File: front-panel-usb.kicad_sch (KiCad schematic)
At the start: 107 parts, among them J4 USB-C_Kycon_KUSBX-SL2-CS1N24-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, J5 Tag-Connect_TC2050-IDC-NL_2x5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, J6 USB-C_Kycon_KUSBX-SL2-CS1N24-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, J7 USB-C_Kycon_KUSBX-SL2-CS1N24-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, Q1 PJE138K, U11 TPD4E05U06QDQARQ1, U12 FT4232H_VQFN, U13 NCP718BSN330T1G, U14 74LVC06ABQ, U15 AP22615B_TSOT26, U16 AP22615B_TSOT26, U17 FUSB303B, U18 FUSB303B, U19 TPD4E05U06QDQARQ1, U20 TPD4E05U06QDQARQ1, Y3 Resonator_12MHz_ABM8G

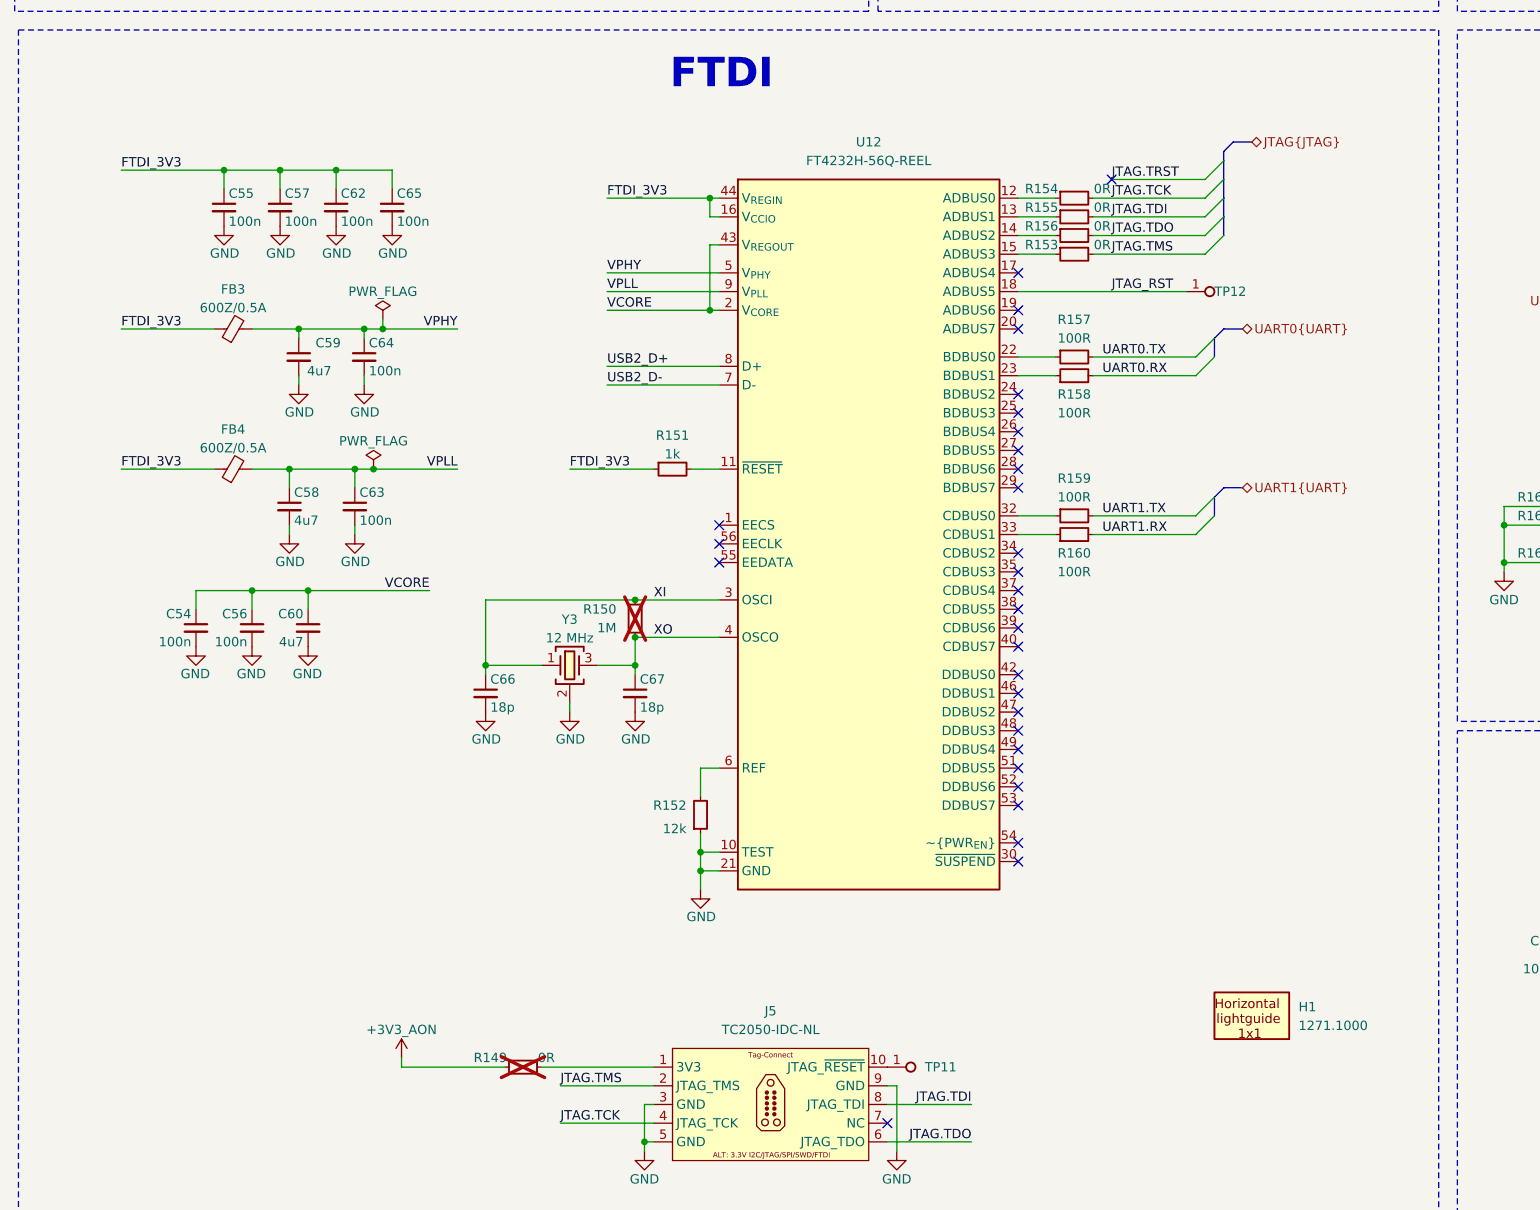
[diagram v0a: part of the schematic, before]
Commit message: [#83767] Add alternative reset signal
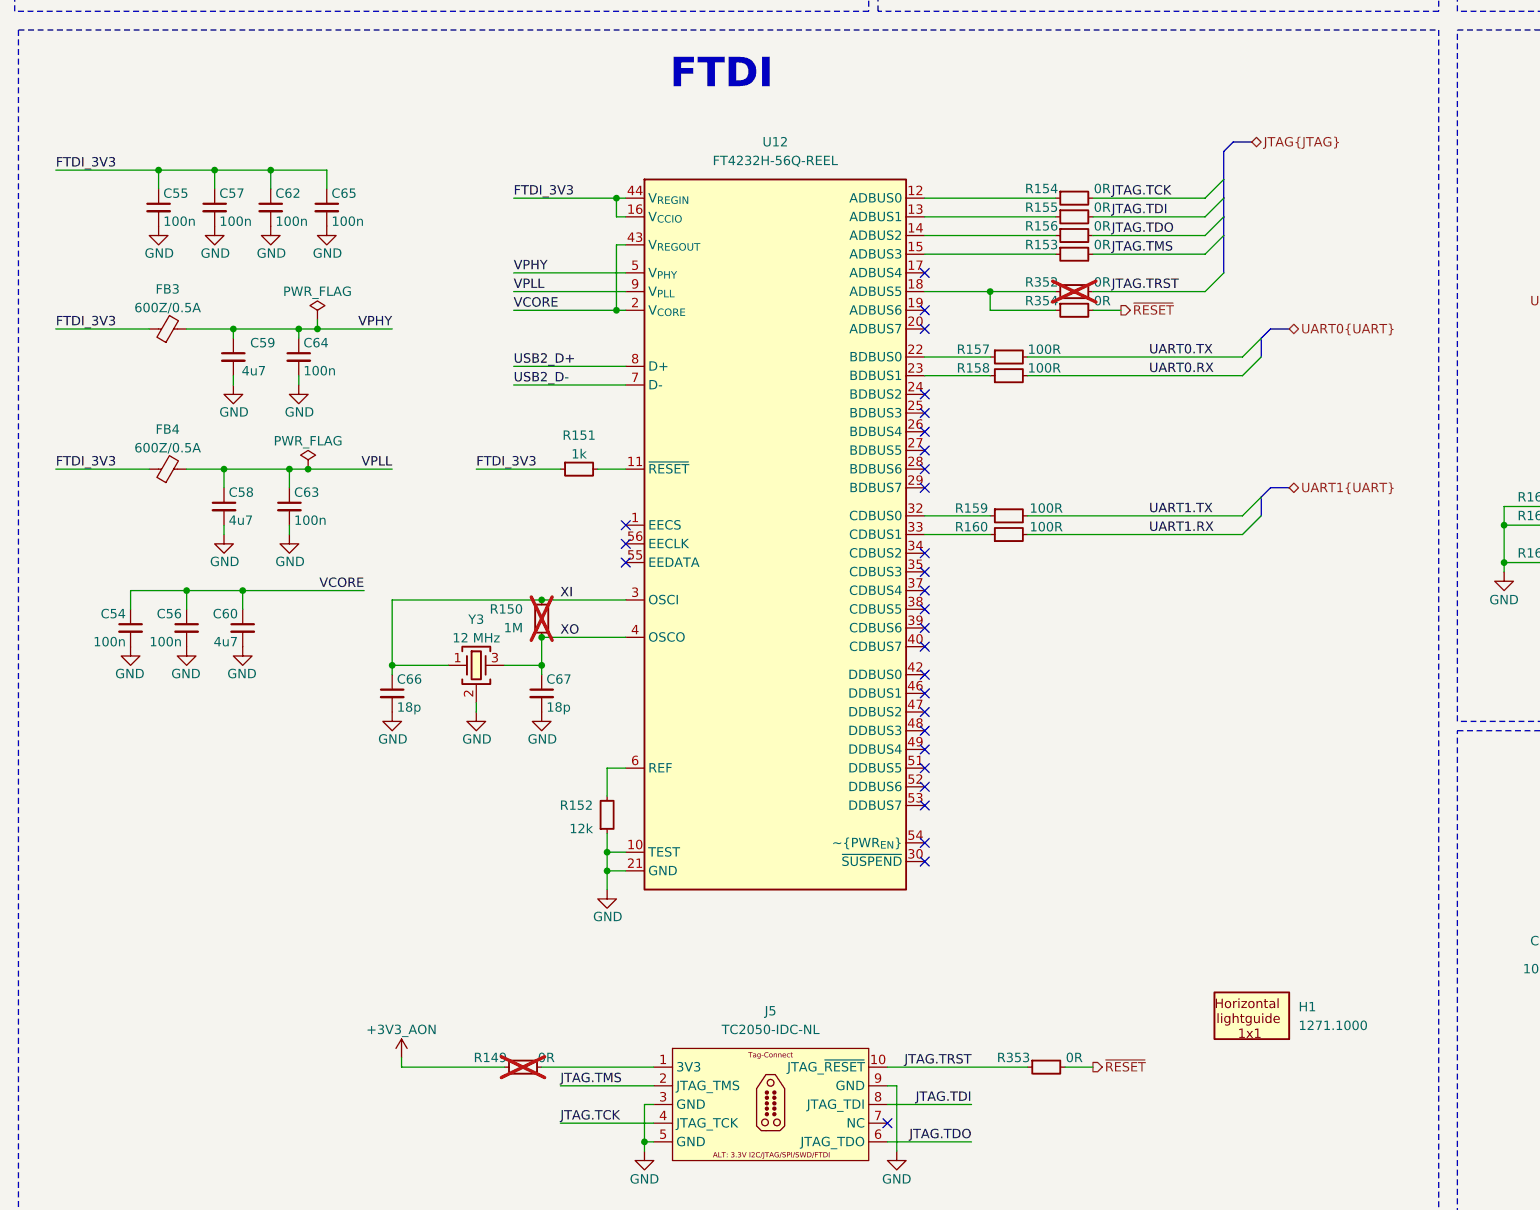
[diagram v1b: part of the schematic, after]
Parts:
- removed TP11, TP12: TP_0.75mm_SMD, antmicro-footprints:TP_SMD_0.75mm, symbol antmicroTestPoints:TP_0.75mm_SMD
- added R352, R353, R354: R_0R_0402, antmicro-footprints:R_0402_1005Metric, symbol antmicroResistors0402:R_0R_0402
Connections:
- net JTAG.TRST: now also J5.10, R352.2, R353.1
- net JTAG_RST: no longer names the net of U12.18 (ADBUS5)
- net JTAG_RST: now also R352.1, R354.1
- new net ~{RESET}: R353.2, R354.2
- no-connect marks 63 -> 62
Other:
- moved on the sheet: C54, C55, C56, C57, C58, C59, C60, C62, C63, C64, C65, C66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

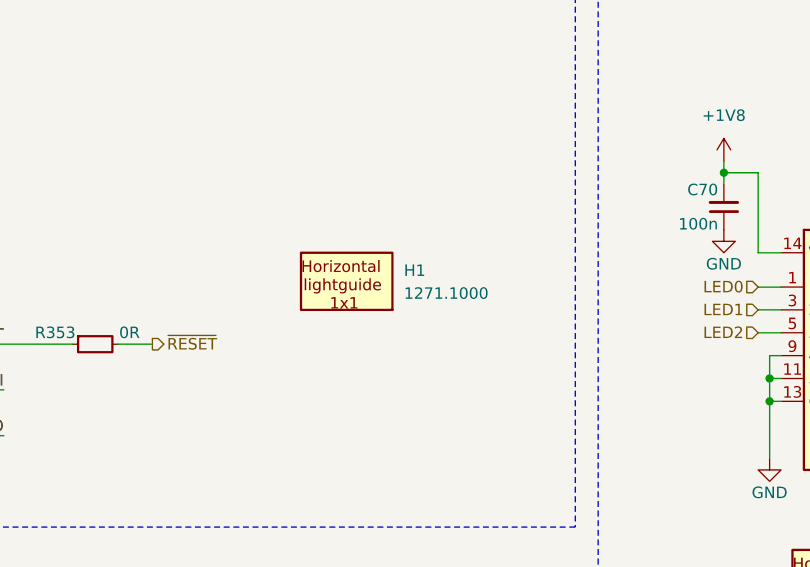
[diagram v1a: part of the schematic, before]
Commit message: [#83767] Remove single lightpipe
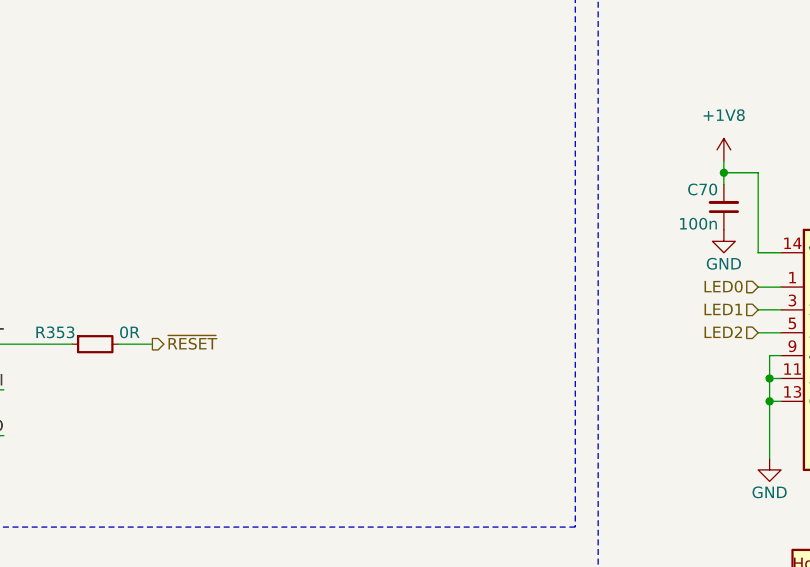
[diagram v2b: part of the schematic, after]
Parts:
- removed H1: Lightpipe_Mentor_1271.1000, antmicro-footprints:Mech_Lightpipe_Mentor_1271.1000, symbol antmicroMechanicalParts:Lightpipe_Mentor_1271.1000
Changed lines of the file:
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@@
-	)
-	(symbol
-		(lib_id "antmicroMechanicalParts:Lightpipe_Mentor_1271.1000")
-		(at 185.42 241.3 0)
-		(unit 1)
-		(exclude_from_sim no)
-		(in_bom yes)
-		(on_board yes)
-		(dnp no)
-		(fields_autoplaced yes)
-		(property "Reference" "H1"
-			(at 191.77 239.4777 0)
-			(effects
-				(font
-					(size 1.27 1.27)
-					(thickness 0.15)
-				)
-				(justify left)
-			)
-		)
-		(property "Value" "Lightpipe_Mentor_1271.1000"
-			(at 205.74 248.92 0)
-			(effects
-				(font
-					(size 1.27 1.27)
-					(thickness 0.15)
-				)
-				(justify left bottom)
-				(hide yes)
-			)
-		)
-		(property "Footprint" "antmicro-footprints:Mech_Lightpipe_Mentor_1271.1000"
-			(at 205.74 251.46 0)
-			(effects
-				(font
-					(size 1.27 1.27)
-					(thickness 0.15)
-				)
-				(justify left bottom)
-				(hide yes)
-			)
-		)
-		(property "Datasheet" "https://www.mentor.de.com/productpdfs/ll/ll14-20.pdf"
-			(at 205.74 254 0)
-			(effects
-				(font
-					(size 1.27 1.27)
-					(thickness 0.15)
-				)
-				(justify left bottom)
-				(hide yes)
-			)
-		)
-		(property "Description" "Light Pipe, Miniature 14.45 mm, 1 Pipe, Circular, PC Board, Transparent"
-			(at 185.42 241.3 0)
-			(effects
-				(font
-					(size 1.27 1.27)
-				)
-				(hide yes)
-			)
-		)
-		(property "Manufacturer" "Mentor Worldwide"
-			(at 205.74 256.54 0)
-			(effects
-				(font
-					(size 1.27 1.27)
-					(thickness 0.15)
-				)
-				(justify left bottom)
-				(hide yes)
-			)
-		)
-		(property "MPN" "1271.1000"
-			(at 191.77 242.0177 0)
-			(effects
-				(font
-					(size 1.27 1.27)
-					(thickness 0.15)
-				)
-				(justify left)
-			)
-		)
-		(property "Author" "Antmicro"
-			(at 205.74 259.08 0)
-			(effects
-				(font
-					(size 1.27 1.27)
-					(thickness 0.15)
-				)
-				(justify left bottom)
-				(hide yes)
-			)
-		)
-		(property "License" "Apache-2.0"
-			(at 205.74 261.62 0)
-			(effects
-				(font
-					(size 1.27 1.27)
-					(thickness 0.15)
-				)
-				(justify left bottom)
-				(hide yes)
-			)
-		)
-		(instances
-			(project "bmc-reference-carrier-board"
-				(path "/5f636c45-3c15-4731-8931-4625e0dab7e4/1d9765f7-f475-4be6-a940-c0038af0d26c"
-					(reference "H1")
-					(unit 1)
-				)
-			)
-		)
 	)
 	(symbol

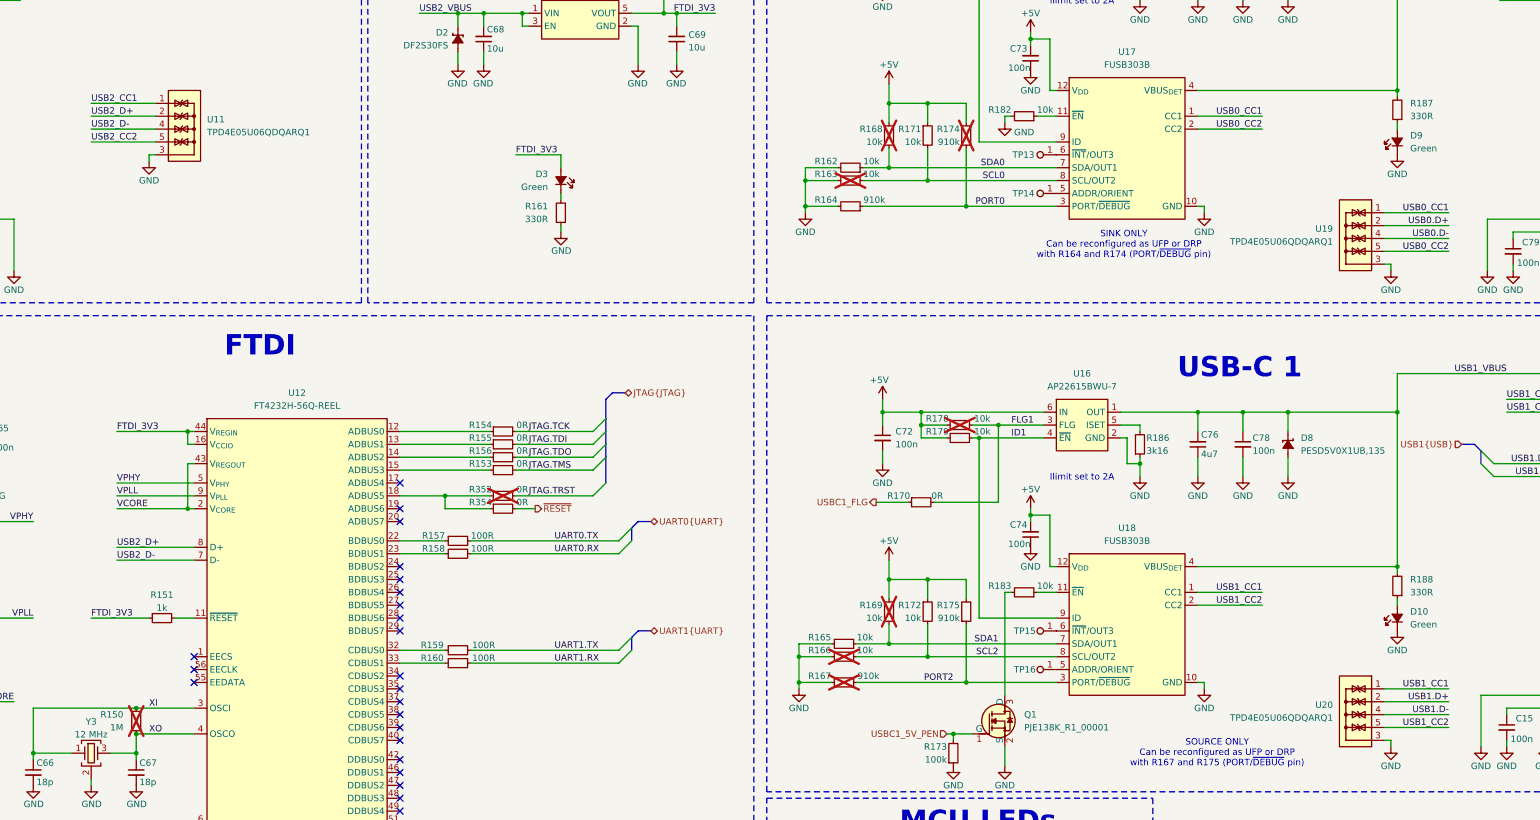
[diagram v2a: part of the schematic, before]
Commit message: [#83767] Connect ESD only to USB data lines
CC lines have ESD inside CC controller
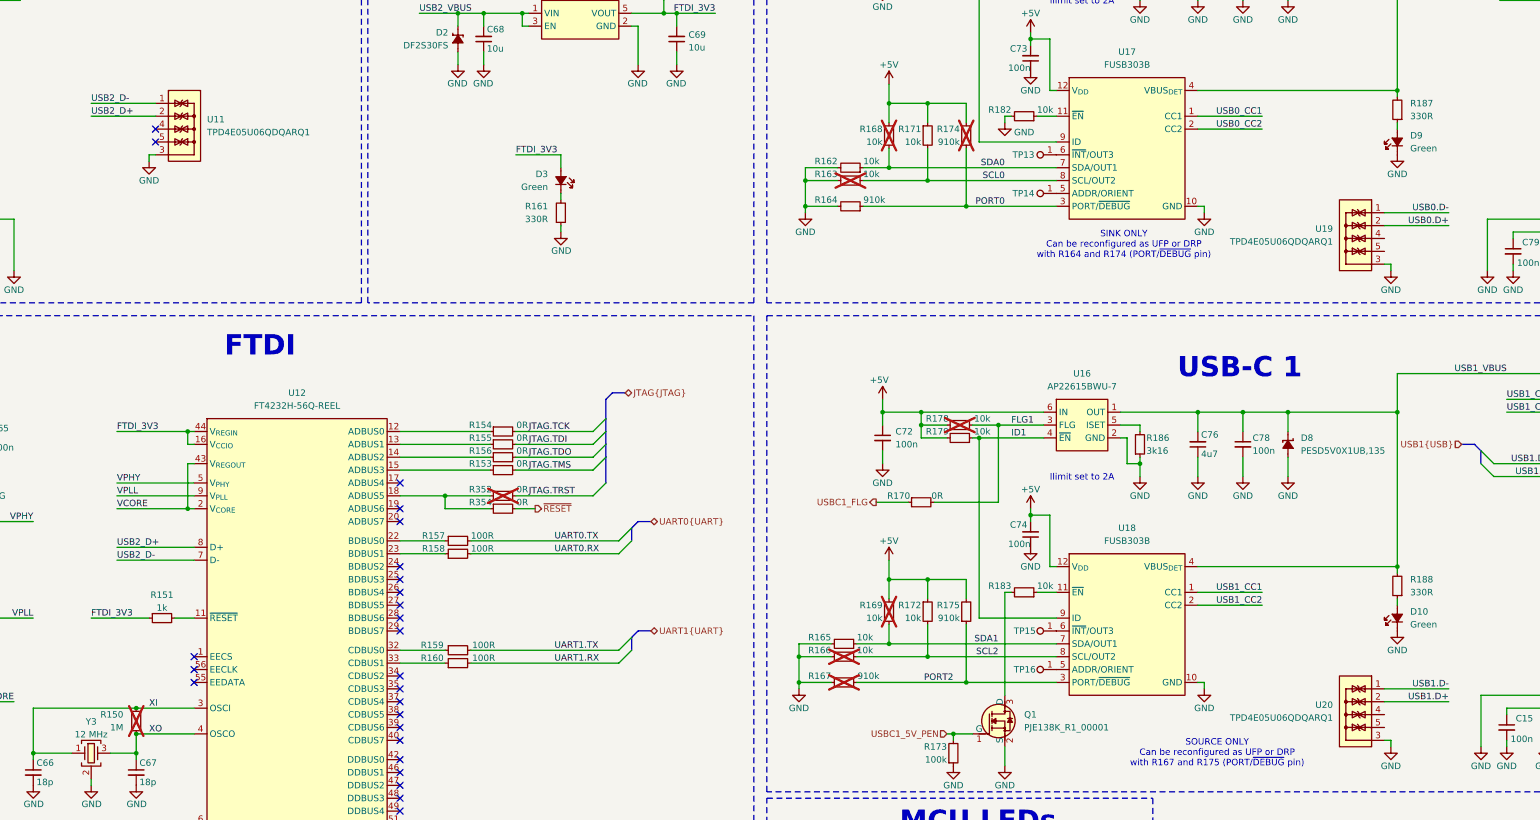
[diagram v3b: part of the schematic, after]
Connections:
- net USB0.D-: now also U19.1, U19.10; no longer U19.4, U19.7
- net USB0_CC1: no longer U19.1, U19.10
- net USB0_CC2: no longer U19.5, U19.6
- net USB1.D-: now also U20.1, U20.10; no longer U20.4, U20.7
- net USB1_CC1: no longer U20.1, U20.10
- net USB1_CC2: no longer U20.5, U20.6
- net USB2_CC1: no longer U11.1, U11.10
- net USB2_CC2: no longer U11.5, U11.6
- net USB2_D-: now also U11.1, U11.10; no longer U11.4, U11.7
- new net: U19.4, U19.7
- new net: U19.5, U19.6
- new net: U20.4, U20.7
- new net: U20.5, U20.6
- new net: U11.4, U11.7
- new net: U11.5, U11.6
- no-connect marks 62 -> 64
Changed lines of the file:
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@@
 	)
 	(no_connect
+		(at 92.71 72.39)
+	)
+	(no_connect
 		(at 48.26 59.69)
 	)
@@
 	)
 	(no_connect
+		(at 92.71 69.85)
+	)
+	(no_connect
 		(at 140.97 201.93)
 	)
@@
 	(wire
 		(pts
-			(xy 80.01 69.85) (xy 92.71 69.85)
+			(xy 80.01 64.77) (xy 92.71 64.77)
 		)
 		(stroke
@@
 	(wire
 		(pts
-			(xy 80.01 64.77) (xy 92.71 64.77)
-		)
-		(stroke
-			(width 0)
-			(type default)
-		)
-	)
-	(wire
-		(pts
 			(xy 245.11 80.01) (xy 270.51 80.01)
 		)
@@
 	(wire
 		(pts
-			(xy 347.98 187.96) (xy 335.28 187.96)
-		)
-		(stroke
-			(width 0)
-			(type default)
-		)
-	)
-	(wire
-		(pts
 			(xy 102.87 259.08) (xy 102.87 257.81)
 		)
@@
 		)
 	)
-	(wire
-		(pts
-			(xy 347.98 86.36) (xy 335.28 86.36)
-		)
-		(stroke
-			(width 0)
-			(type default)
-		)
-	)
 	(bus
 		(pts
@@
 	(wire
 		(pts
-			(xy 347.98 180.34) (xy 335.28 180.34)
-		)
-		(stroke
-			(width 0)
-			(type default)
-		)
-	)
-	(wire
-		(pts
 			(xy 140.97 175.26) (xy 149.86 175.26)
 		)
@@
 	(wire
 		(pts
-			(xy 347.98 93.98) (xy 335.28 93.98)
-		)
-		(stroke
-			(width 0)
-			(type default)
-		)
-	)
-	(wire
-		(pts
 			(xy 248.92 36.83) (xy 243.84 36.83)
 		)
@@
 	(wire
 		(pts
-			(xy 347.98 91.44) (xy 335.28 91.44)
+			(xy 347.98 86.36) (xy 335.28 86.36)
 		)
 		(stroke
@@
 	(wire
 		(pts
-			(xy 347.98 185.42) (xy 335.28 185.42)
-		)
-		(stroke
-			(width 0)
-			(type default)
-		)
-	)
-	(wire
-		(pts
-			(xy 80.01 72.39) (xy 92.71 72.39)
+			(xy 347.98 180.34) (xy 335.28 180.34)
 		)
 		(stroke
@@
 	)
 	(label "USB0.D-"
-		(at 347.98 91.44 180)
+		(at 347.98 86.36 180)
 		(effects
 			(font
@@
 		)
 	)
-	(label "USB0_CC1"
-		(at 347.98 86.36 180)
-		(effects
-			(font
-				(size 1.27 1.27)
-			)
-			(justify right bottom)
-		)
-	)
 	(label "PORT2"
 		(at 250.19 179.07 180)
@@
 	)
 	(label "USB1.D-"
-		(at 347.98 185.42 180)
+		(at 347.98 180.34 180)
 		(effects
 			(font
@@
 		)
 	)
-	(label "USB2_CC2"
-		(at 80.01 72.39 0)
-		(effects
-			(font
-				(size 1.27 1.27)
-			)
-			(justify left bottom)
-		)
-	)
 	(label "USB1_CC2"
 		(at 311.15 163.83 180)
@@
 		)
 	)
-	(label "USB1_CC1"
-		(at 347.98 180.34 180)
-		(effects
-			(font
-				(size 1.27 1.27)
-			)
-			(justify right bottom)
-		)
-	)
 	(label "FTDI_3V3"
 		(at 22.86 125.73 0)
@@
 		)
 	)
-	(label "USB1_CC2"
-		(at 347.98 187.96 180)
-		(effects
-			(font
-				(size 1.27 1.27)
-			)
-			(justify right bottom)
-		)
-	)
 	(label "USB2_VBUS"
 		(at 144.78 46.99 0)
@@
 	)
 	(label "USB2_D-"
-		(at 80.01 69.85 0)
+		(at 80.01 64.77 0)
 		(effects
 			(font
@@
 		)
 	)
-	(label "USB0_CC2"
-		(at 347.98 93.98 180)
-		(effects
-			(font
-				(size 1.27 1.27)
-			)
-			(justify right bottom)
-		)
-	)
 	(label "PORT0"
 		(at 260.35 85.09 180)
@@
 		(effects
 			(font
-				(size 1.27 1.27)
-			)
-			(justify left bottom)
-		)
-	)
-	(label "USB2_CC1"
-		(at 80.01 64.77 0)
-		(effects
-			(font
